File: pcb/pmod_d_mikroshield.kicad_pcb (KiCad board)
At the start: 2 copper layers, 25.4 x 28.6 mm, 9 parts, among them J1 CON_HDR_MIKROBUS_ADDON_TH, J2 CON_HDR_100MILS_F_TH_RA_2X6, J3 CON_HDR_100MILS_M_TH_1X3, J4 CON_HDR_100MILS_M_TH_1X2, J5 CON_HDR_100MILS_M_TH_1X2

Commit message: Add oshw logo.
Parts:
- added G***: LOGO, LOGO, F.Cu at (129.5, 101.6)

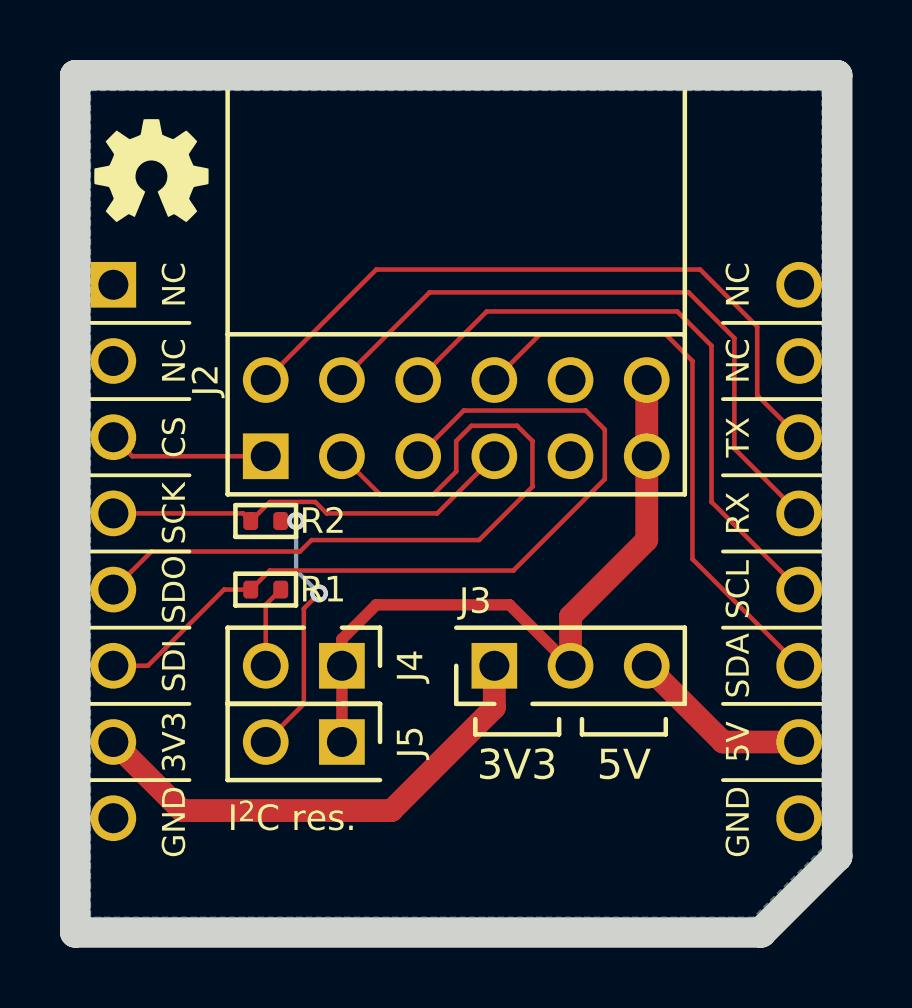
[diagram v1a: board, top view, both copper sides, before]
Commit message: Silkscreen fixes
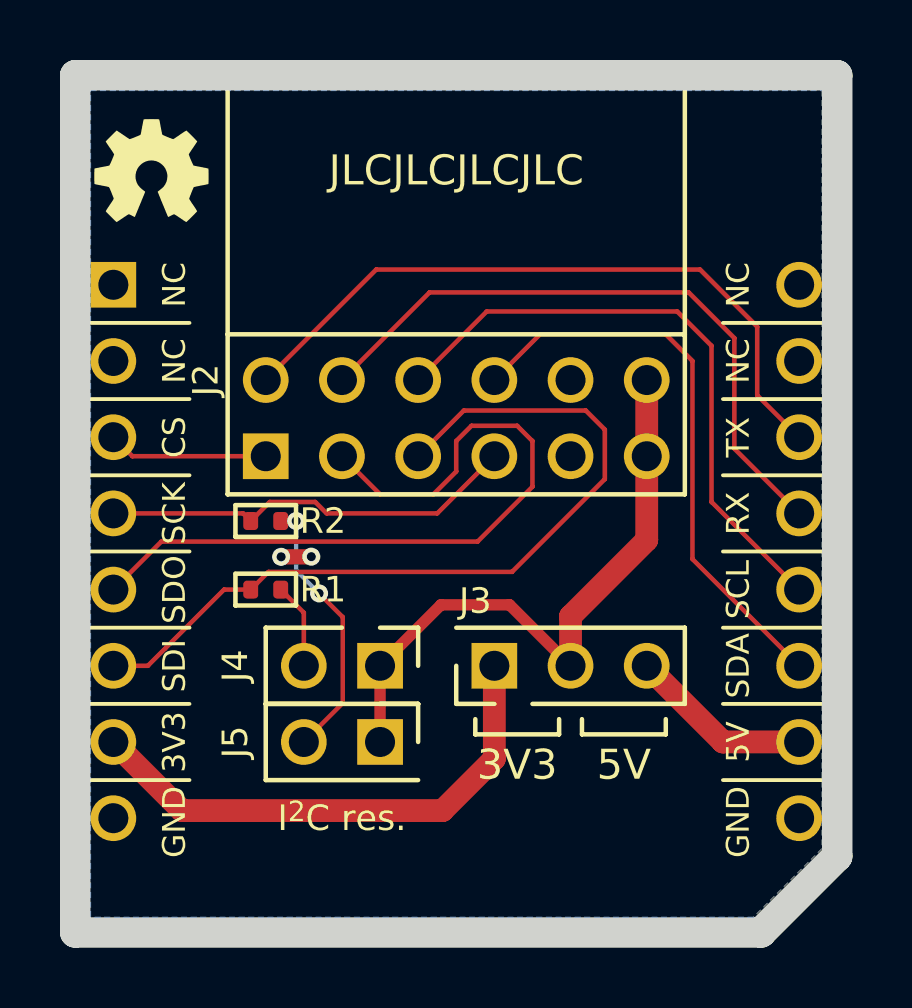
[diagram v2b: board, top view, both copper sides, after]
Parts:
- moved J4 1.27 mm to (135.9, 118.1)
- moved J5 1.27 mm to (135.9, 120.7)
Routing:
- net /VCC: track 22.9 -> 21.2 mm
- net GND: track 0.00 -> 1.01 mm, vias 0 -> 2
- net +3.3VA: track 16.5 -> 17.5 mm
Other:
- board text added: "JLCJLCJLCJLC"
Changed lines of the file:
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@@
     (grid_origin 127 127)
     (pcbplotparams
-      (layerselection 0x00010fc_ffffffff)
+      (layerselection 0x00010f8_ffffffff)
       (disableapertmacros false)
       (usegerberextensions false)
@@
       (outputformat 1)
       (mirror false)
-      (drillshape 1)
+      (drillshape 0)
       (scaleselection 1)
-      (outputdirectory "")
+      (outputdirectory "../out")
     )
   )
@@
   )
   (footprint "connaxio-connectors:CON_HDR_100MILS_M_TH_1X2" (layer "F.Cu")
-    (at 134.62 118.11 -90)
+    (at 135.89 118.11 -90)
     (descr "Through hole straight pin header, 1x02, 2.54mm pitch, single row")
     (tags "Through hole pin header THT 1x02 2.54mm single row")
@@
     (solder_mask_margin 0.05)
     (attr through_hole)
-    (fp_text reference "J4" (at 0 -3.556 90) (layer "F.SilkS")
+    (fp_text reference "J4" (at 0 3.556 90) (layer "F.SilkS")
       (effects (font (size 0.85 0.85) (thickness 0.15)))
     )
@@
   )
   (footprint "connaxio-connectors:CON_HDR_100MILS_M_TH_1X2" (layer "F.Cu")
-    (at 134.62 120.65 -90)
+    (at 135.89 120.65 -90)
     (descr "Through hole straight pin header, 1x02, 2.54mm pitch, single row")
     (tags "Through hole pin header THT 1x02 2.54mm single row")
@@
     (solder_mask_margin 0.05)
     (attr through_hole)
-    (fp_text reference "J5" (at 0 -3.556 90) (layer "F.SilkS")
+    (fp_text reference "J5" (at 0 3.556 90) (layer "F.SilkS")
       (effects (font (size 0.85 0.85) (thickness 0.15)))
     )
@@
     (effects (font (size 1 1) (thickness 0.15)))
   )
-  (gr_text "I^{2}C res." (at 132.08 123.19) (layer "F.SilkS")
-    (effects (font (size 0.85 0.85) (thickness 0.15)) (justify left))
+  (gr_text "JLCJLCJLCJLC" (at 139.7 101.6) (layer "F.SilkS")
+    (effects (font (size 1 1) (thickness 0.15)))
+  )
+  (gr_text "I^{2}C res." (at 135.89 123.19) (layer "F.SilkS")
+    (effects (font (size 0.85 0.85) (thickness 0.15)))
   )
   (gr_text "5V" (at 145.288 121.412) (layer "F.SilkS")
@@
   (segment (start 132.85 113.284) (end 132.596 113.03) (width 0.1524) (layer "F.Cu") (net 2))
   (segment (start 132.596 113.03) (end 128.27 113.03) (width 0.1524) (layer "F.Cu") (net 2))
+  (segment (start 137.16 112.395) (end 138.938 112.395) (width 0.1524) (layer "F.Cu") (net 3))
+  (segment (start 139.7 111.633) (end 139.7 110.617) (width 0.1524) (layer "F.Cu") (net 3))
   (segment (start 142.24 110.617) (end 142.24 112.141) (width 0.1524) (layer "F.Cu") (net 3))
+  (segment (start 142.24 112.141) (end 140.4112 113.9698) (width 0.1524) (layer "F.Cu") (net 3))
+  (segment (start 141.732 110.109) (end 142.24 110.617) (width 0.1524) (layer "F.Cu") (net 3))
+  (segment (start 140.208 110.109) (end 141.732 110.109) (width 0.1524) (layer "F.Cu") (net 3))
+  (segment (start 139.7 110.617) (end 140.208 110.109) (width 0.1524) (layer "F.Cu") (net 3))
   (segment (start 138.938 112.395) (end 139.7 111.633) (width 0.1524) (layer "F.Cu") (net 3))
-  (segment (start 140.208 110.109) (end 141.732 110.109) (width 0.1524) (layer "F.Cu") (net 3))
-  (segment (start 134.493 114.3) (end 129.54 114.3) (width 0.1524) (layer "F.Cu") (net 3))
-  (segment (start 142.24 112.141) (end 140.462 113.919) (width 0.1524) (layer "F.Cu") (net 3))
+  (segment (start 129.8702 113.9698) (end 128.27 115.57) (width 0.1524) (layer "F.Cu") (net 3))
   (segment (start 135.89 111.125) (end 137.16 112.395) (width 0.1524) (layer "F.Cu") (net 3))
-  (segment (start 141.732 110.109) (end 142.24 110.617) (width 0.1524) (layer "F.Cu") (net 3))
-  (segment (start 137.16 112.395) (end 138.938 112.395) (width 0.1524) (layer "F.Cu") (net 3))
-  (segment (start 140.462 113.919) (end 134.874 113.919) (width 0.1524) (layer "F.Cu") (net 3))
-  (segment (start 134.874 113.919) (end 134.493 114.3) (width 0.1524) (layer "F.Cu") (net 3))
-  (segment (start 139.7 110.617) (end 140.208 110.109) (width 0.1524) (layer "F.Cu") (net 3))
-  (segment (start 129.54 114.3) (end 128.27 115.57) (width 0.1524) (layer "F.Cu") (net 3))
-  (segment (start 139.7 111.633) (end 139.7 110.617) (width 0.1524) (layer "F.Cu") (net 3))
+  (segment (start 140.4112 113.9698) (end 129.8702 113.9698) (width 0.1524) (layer "F.Cu") (net 3))
+  (segment (start 141.559489 114.980511) (end 133.439489 114.980511) (width 0.1524) (layer "F.Cu") (net 4))
+  (segment (start 144.653 111.887) (end 141.559489 114.980511) (width 0.1524) (layer "F.Cu") (net 4))
+  (segment (start 144.018 109.601) (end 144.653 110.236) (width 0.1524) (layer "F.Cu") (net 4))
   (segment (start 132.85 115.57) (end 131.961 115.57) (width 0.1524) (layer "F.Cu") (net 4))
-  (segment (start 138.43 111.125) (end 139.954 109.601) (width 0.1524) (layer "F.Cu") (net 4))
-  (segment (start 144.018 109.601) (end 144.653 110.236) (width 0.1524) (layer "F.Cu") (net 4))
+  (segment (start 144.653 110.236) (end 144.653 111.887) (width 0.1524) (layer "F.Cu") (net 4))
   (segment (start 129.421 118.11) (end 128.27 118.11) (width 0.1524) (layer "F.Cu") (net 4))
   (segment (start 129.9885 117.5425) (end 129.421 118.11) (width 0.1524) (layer "F.Cu") (net 4))
-  (segment (start 141.605 114.935) (end 133.485 114.935) (width 0.1524) (layer "F.Cu") (net 4))
-  (segment (start 144.653 111.887) (end 141.605 114.935) (width 0.1524) (layer "F.Cu") (net 4))
+  (segment (start 133.439489 114.980511) (end 132.85 115.57) (width 0.1524) (layer "F.Cu") (net 4))
+  (segment (start 138.43 111.125) (end 139.954 109.601) (width 0.1524) (layer "F.Cu") (net 4))
+  (segment (start 139.954 109.601) (end 144.018 109.601) (width 0.1524) (layer "F.Cu") (net 4))
   (segment (start 131.961 115.57) (end 129.9885 117.5425) (width 0.1524) (layer "F.Cu") (net 4))
-  (segment (start 144.653 110.236) (end 144.653 111.887) (width 0.1524) (layer "F.Cu") (net 4))
-  (segment (start 139.954 109.601) (end 144.018 109.601) (width 0.1524) (layer "F.Cu") (net 4))
-  (segment (start 133.485 114.935) (end 132.85 115.57) (width 0.1524) (layer "F.Cu") (net 4))
-  (segment (start 140.97 119.507) (end 140.97 118.11) (width 0.762) (layer "F.Cu") (net 5))
-  (segment (start 137.541 122.936) (end 140.97 119.507) (width 0.762) (layer "F.Cu") (net 5))
-  (segment (start 130.556 122.936) (end 137.541 122.936) (width 0.762) (layer "F.Cu") (net 5))
+  (segment (start 140.97 121.2088) (end 140.97 118.11) (width 0.762) (layer "F.Cu") (net 5))
   (segment (start 128.27 120.65) (end 130.556 122.936) (width 0.762) (layer "F.Cu") (net 5))
+  (segment (start 139.2428 122.936) (end 140.97 121.2088) (width 0.762) (layer "F.Cu") (net 5))
+  (segment (start 130.556 122.936) (end 139.2428 122.936) (width 0.762) (layer "F.Cu") (net 5))
+  (segment (start 133.8633 114.477811) (end 134.863389 114.477811) (width 0.508) (layer "F.Cu") (net 6))
+  (segment (start 134.863389 114.477811) (end 134.8687 114.4725) (width 0.508) (layer "F.Cu") (net 6))
+  (via (at 134.8687 114.4725) (size 0.6) (drill 0.3) (layers "F.Cu" "B.Cu") (free) (net 6))
+  (via (at 133.8633 114.477811) (size 0.6) (drill 0.3) (layers "F.Cu" "B.Cu") (free) (net 6))
   (segment (start 151.13 110.49) (end 149.733 109.093) (width 0.1524) (layer "F.Cu") (net 7))
   (segment (start 147.828 104.902) (end 137.033 104.902) (width 0.1524) (layer "F.Cu") (net 7))
@@
   (segment (start 151.13 120.65) (end 148.59 120.65) (width 0.762) (layer "F.Cu") (net 11))
   (segment (start 148.59 120.65) (end 146.05 118.11) (width 0.762) (layer "F.Cu") (net 11))
-  (segment (start 135.89 118.11) (end 135.89 117.221) (width 0.381) (layer "F.Cu") (net 12))
-  (segment (start 135.89 117.221) (end 137.033 116.078) (width 0.381) (layer "F.Cu") (net 12))
   (segment (start 146.05 108.585) (end 146.05 111.125) (width 0.762) (layer "F.Cu") (net 12))
+  (segment (start 139.192 116.078) (end 137.16 118.11) (width 0.381) (layer "F.Cu") (net 12))
+  (segment (start 137.16 118.11) (end 137.16 120.65) (width 0.381) (layer "F.Cu") (net 12))
   (segment (start 146.05 113.919) (end 146.05 111.125) (width 0.762) (layer "F.Cu") (net 12))
-  (segment (start 137.033 116.078) (end 141.478 116.078) (width 0.381) (layer "F.Cu") (net 12))
-  (segment (start 135.89 120.65) (end 135.89 118.11) (width 0.381) (layer "F.Cu") (net 12))
+  (segment (start 141.478 116.078) (end 139.192 116.078) (width 0.381) (layer "F.Cu") (net 12))
   (segment (start 143.51 116.459) (end 146.05 113.919) (width 0.762) (layer "F.Cu") (net 12))
   (segment (start 143.51 118.11) (end 143.51 116.459) (width 0.762) (layer "F.Cu") (net 12))
   (segment (start 141.478 116.078) (end 143.51 118.11) (width 0.381) (layer "F.Cu") (net 12))
-  (segment (start 133.85 115.57) (end 133.35 116.07) (width 0.1524) (layer "F.Cu") (net 13))
-  (segment (start 133.35 116.07) (end 133.35 118.11) (width 0.1524) (layer "F.Cu") (net 13))
-  (segment (start 134.62 116.205) (end 135.128 115.697) (width 0.1524) (layer "F.Cu") (net 14))
-  (segment (start 134.62 119.38) (end 134.62 116.84) (width 0.1524) (layer "F.Cu") (net 14))
-  (segment (start 134.62 116.84) (end 134.62 116.205) (width 0.1524) (layer "F.Cu") (net 14))
+  (segment (start 134.62 118.11) (end 134.62 116.34) (width 0.1524) (layer "F.Cu") (net 13))
+  (segment (start 134.62 116.34) (end 133.85 115.57) (width 0.1524) (layer "F.Cu") (net 13))
+  (segment (start 135.128 115.697) (end 135.9154 116.4844) (width 0.1524) (layer "F.Cu") (net 14))
+  (segment (start 135.9154 119.3546) (end 134.62 120.65) (width 0.1524) (layer "F.Cu") (net 14))
+  (segment (start 135.9154 116.4844) (end 135.9154 119.3546) (width 0.1524) (layer "F.Cu") (net 14))
   (segment (start 133.85 113.284) (end 134.366 113.284) (width 0.1524) (layer "F.Cu") (net 14))
-  (segment (start 133.35 120.65) (end 134.62 119.38) (width 0.1524) (layer "F.Cu") (net 14))
   (via (at 134.366 113.284) (size 0.6) (drill 0.3) (layers "F.Cu" "B.Cu") (net 14))
   (via (at 135.128 115.697) (size 0.6) (drill 0.3) (layers "F.Cu" "B.Cu") (net 14))
